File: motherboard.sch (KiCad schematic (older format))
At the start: 90 parts, among them P1 CONN_02X08, U1 STM32F411-LQFP64, U10 74LS125, U11 74LS125, U12 74LS125, U13 74LS125, U14 PCA9517A, U15 PCA9517A, U16 74LS125, U17 74LS125, U2 STM32F411-LQFP64, U3 AP7313, U4 74LS00, U5 74LS125, U6 FM25V20A-G, U7 FM25V20A-G, U8 FM25V20A-G, U9 FM25V20A-G, Y1 32k, Y2 8M(16pF), Y3 32k, Y4 8M(16pF)

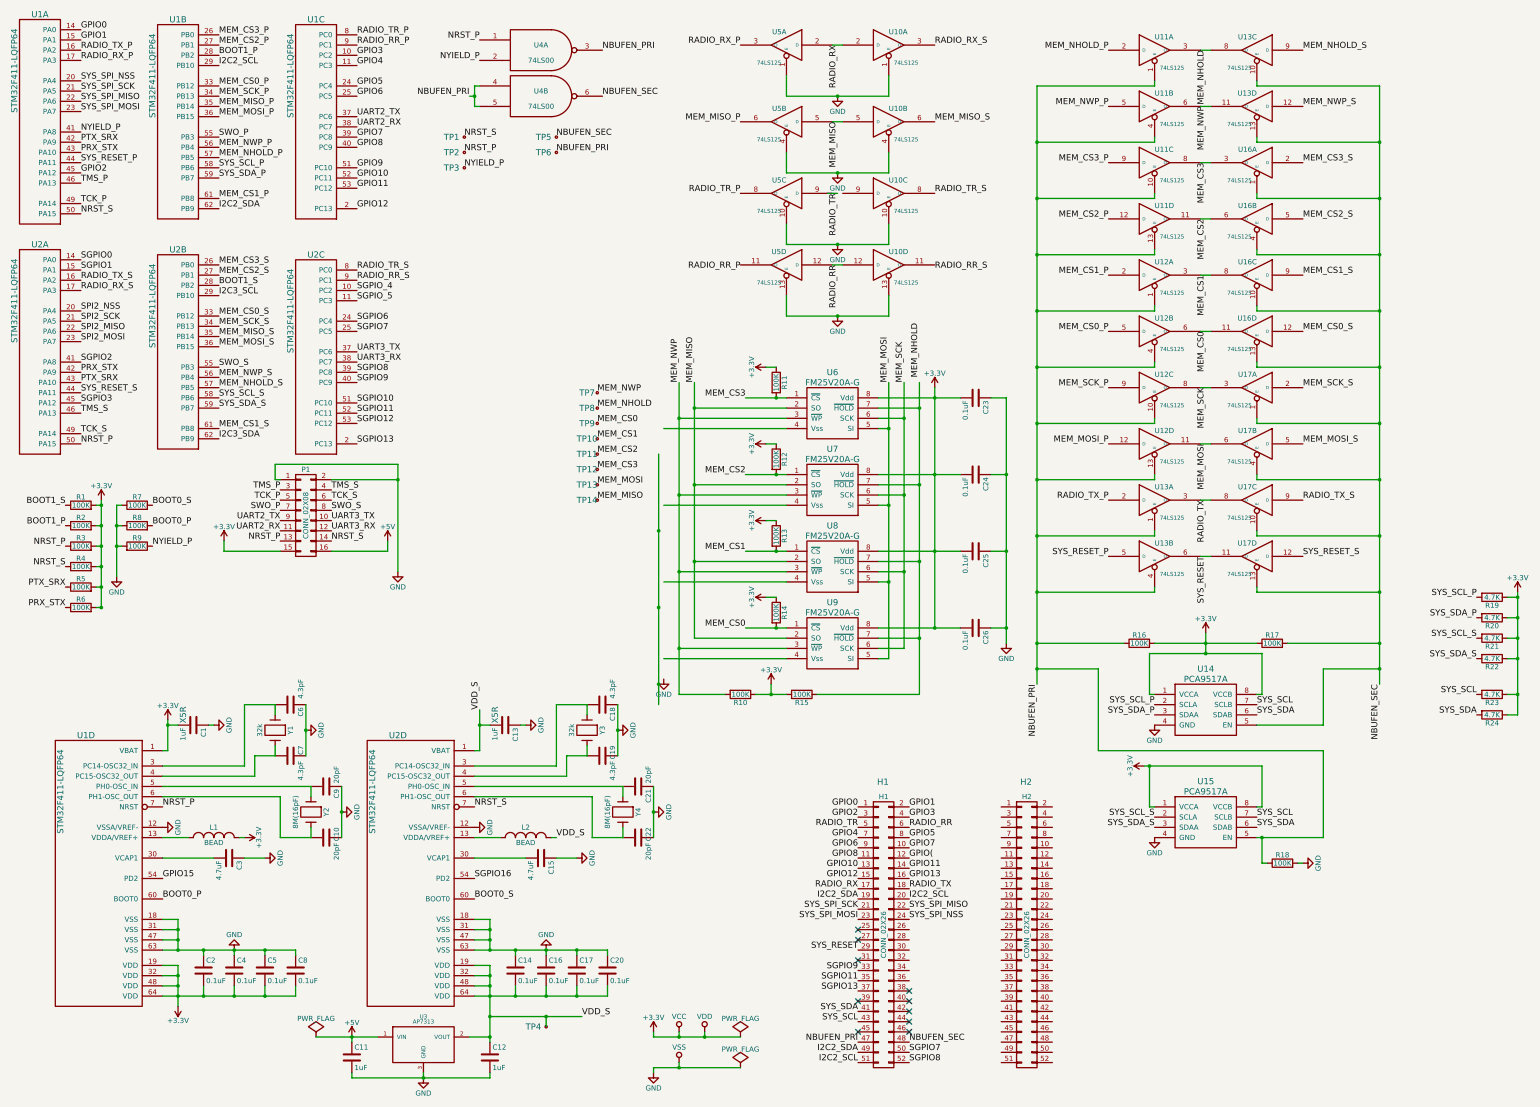
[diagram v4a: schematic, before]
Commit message: Schematic passes DRC
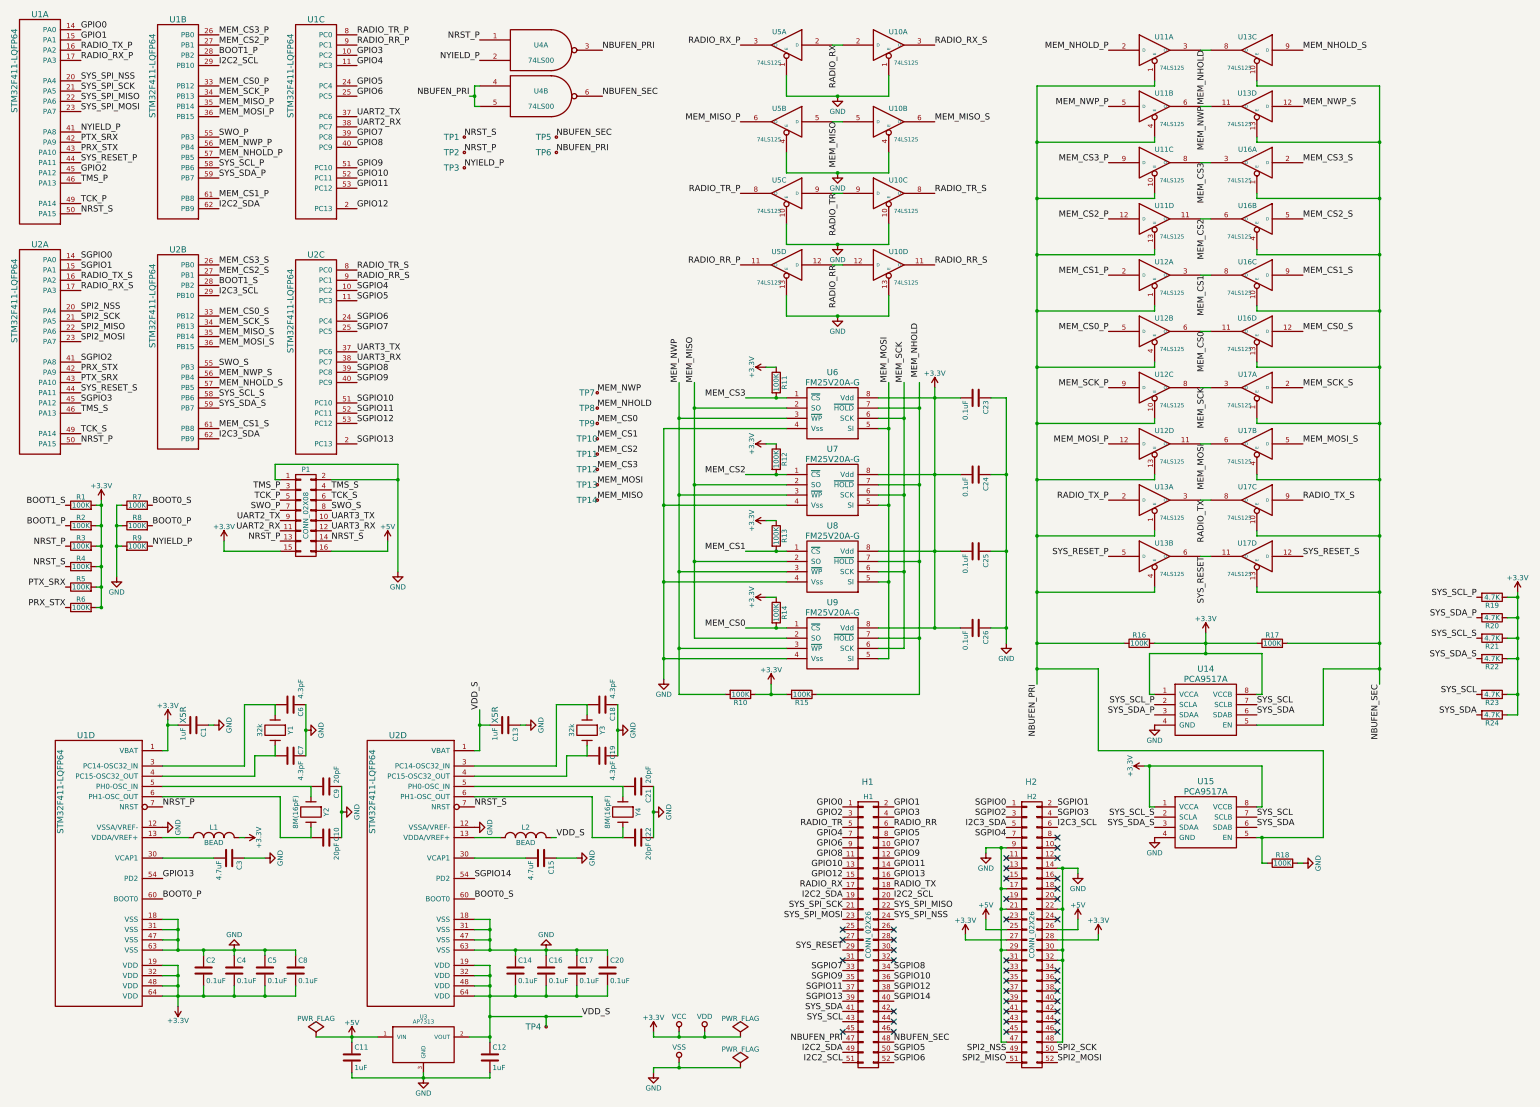
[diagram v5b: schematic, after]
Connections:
- net GPIO( is gone; now on net GPIO9: H1.12 (P12)
- net GPIO15 is gone; now on net GPIO13: U1.54 (PD2)
- net SGPIO16 is gone; now on net SGPIO14: U2.54 (PD2)
- net SGPIO_4 is gone; now on net SGPIO4: U2.10 (PC2)
- net +3V3: now also H2.27 (P27), H2.28 (P28)
- net +5V: now also H2.25 (P25), H2.26 (P26)
- net GND: now also H2.14 (P14), H2.17 (P17), H2.21 (P21), H2.22 (P22), H2.29 (P29), H2.30 (P30), H2.32 (P32), H2.47 (P47), H2.48 (P48), H2.9 (P9), U6.4 (Vss), U7.4 (Vss), U8.4 (Vss), U9.4 (Vss)
- net I2C3_SCL: now also H2.6 (P6)
- net I2C3_SDA: now also H2.5 (P5)
- net RADIO_RR_P: now also U5.11 (O)
- net RADIO_RR_S: now also U10.11 (O)
- net RADIO_TR: now also U10.9 (D), U5.9 (D)
- net SGPIO0: now also H2.1 (P1)
- net SGPIO1: now also H2.2 (P2)
- net SGPIO10: now also H1.36 (P36)
- net SGPIO11: now also H1.37 (P37); no longer H1.35 (P35)
- net SGPIO12: now also H1.38 (P38)
- net SGPIO13: now also H1.39 (P39); no longer H1.37 (P37)
- net SGPIO2: now also H2.3 (P3)
- net SGPIO3: now also H2.4 (P4)
- net SGPIO6: now also H1.52 (P52)
- net SGPIO7: now also H1.33 (P33); no longer H1.50 (P50)
- net SGPIO8: now also H1.34 (P34); no longer H1.52 (P52)
- net SGPIO9: now also H1.35 (P35); no longer H1.33 (P33)
- net SPI2_MISO: now also H2.51 (P51)
- net SPI2_MOSI: now also H2.52 (P52)
- net SPI2_NSS: now also H2.49 (P49)
- net SPI2_SCK: now also H2.50 (P50)
- net SGPIO14: now reaches H1.40 (P40)
- net SGPIO4: now reaches H2.7 (P7)
- net SGPIO_5 renamed SGPIO5
- net SGPIO5: now also H1.50 (P50)
- no-connect marks 10 -> 38
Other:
- moved on the sheet: H1, H2

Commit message: Progress in laying out components
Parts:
- renumbered U17 to U10, U5 to U11, U12 to U11, U13 to U11, U10 to U12, U17 to U12, U11 to U13, U11 to U17, U12 to U17, U13 to U5
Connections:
- net GND: now also U10.10 (E), U10.4 (E), U11.1 (E), U12.1 (E), U5.10 (E), U5.4 (E); no longer U10.10 (E), U10.13 (E), U11.4 (E), U12.4 (E), U5.10 (E), U5.13 (E)
- net MEM_CS0: now also U17.11 (O); no longer U17.6 (O)
- net MEM_CS0_P: now also U17.12 (D); no longer U17.5 (D)
- net MEM_CS1: now also U17.8 (O); no longer U17.3 (O)
- net MEM_CS1_P: now also U17.9 (D); no longer U17.2 (D)
- net MEM_CS2: now also U17.6 (O); no longer U17.11 (O)
- net MEM_CS2_P: now also U17.5 (D); no longer U17.12 (D)
- net MEM_CS3: now also U17.3 (O); no longer U17.8 (O)
- net MEM_CS3_P: now also U17.2 (D); no longer U17.9 (D)
- net MEM_MISO: now also U11.2 (D), U12.2 (D); no longer U11.5 (D), U12.5 (D)
- net MEM_MISO_P: now also U11.3 (O); no longer U11.6 (O)
- net MEM_MISO_S: now also U12.3 (O); no longer U12.6 (O)
- net MEM_MOSI: now also U11.8 (O), U12.8 (O); no longer U11.11 (O), U12.6 (O)
- net MEM_MOSI_P: now also U11.9 (D); no longer U11.12 (D)
- net MEM_MOSI_S: now also U12.9 (D); no longer U12.5 (D)
- net MEM_SCK: now also U11.6 (O), U12.6 (O); no longer U11.8 (O), U12.3 (O)
- net MEM_SCK_P: now also U11.5 (D); no longer U11.9 (D)
- net MEM_SCK_S: now also U12.5 (D); no longer U12.2 (D)
- net NBUFEN_PRI: now also U11.10 (E), U11.13 (E), U11.4 (E), U17.1 (E), U17.10 (E), U17.13 (E), U17.4 (E), U5.13 (E); no longer U11.10 (E), U11.13 (E), U11.4 (E), U17.1 (E), U17.10 (E), U17.13 (E), U17.4 (E), U5.1 (E)
- net NBUFEN_SEC: now also U10.13 (E), U12.10 (E), U12.4 (E); no longer U10.10 (E), U12.1 (E), U12.4 (E)
- net RADIO_RR: now also U10.9 (D), U5.9 (D); no longer U10.12 (D), U5.12 (D)
- net RADIO_RR_P: now also U5.8 (O); no longer U5.11 (O)
- net RADIO_RR_S: now also U10.8 (O); no longer U10.11 (O)
- net RADIO_TR: now also U10.5 (D), U5.5 (D); no longer U10.9 (D), U5.9 (D)
- net RADIO_TR_P: now also U5.6 (O); no longer U5.8 (O)
- net RADIO_TR_S: now also U10.6 (O); no longer U10.8 (O)
- net RADIO_TX: now also U10.11 (O), U5.11 (O); no longer U10.8 (O), U5.3 (O)
- net RADIO_TX_P: now also U5.12 (D); no longer U5.2 (D)
- net RADIO_TX_S: now also U10.12 (D); no longer U10.9 (D)
- net SYS_RESET: now also U11.11 (O); no longer U11.6 (O)
- net SYS_RESET_P: now also U11.12 (D); no longer U11.5 (D)
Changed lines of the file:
@@
 $EndComp
 $Comp
-L 74LS125 U5
-U 2 1 56F0C25F
+L 74LS125 U11
+U 1 1 56F0C25F
 P 8350 1650
-F 0 "U5" H 8350 1750 50  0000 L BNN
+F 0 "U11" H 8350 1750 50  0000 L BNN
 F 1 "74LS125" H 8400 1500 40  0000 L TNN
 F 2 "Housings_SOIC:SOIC-14_3.9x8.7mm_Pitch1.27mm" H 8350 1650 60  0001 C CNN
 F 3 "" H 8350 1650 60  0000 C CNN
-	2    8350 1650
-	-1   0    0    -1
-$EndComp
-$Comp
-L 74LS125 U10
-U 2 1 56F0C346
+	1    8350 1650
+	-1   0    0    -1
+$EndComp
+$Comp
+L 74LS125 U12
+U 1 1 56F0C346
 P 9350 1650
-F 0 "U10" H 9350 1750 50  0000 L BNN
+F 0 "U12" H 9350 1750 50  0000 L BNN
 F 1 "74LS125" H 9400 1500 40  0000 L TNN
 F 2 "Housings_SOIC:SOIC-14_3.9x8.7mm_Pitch1.27mm" H 9350 1650 60  0001 C CNN
 F 3 "" H 9350 1650 60  0000 C CNN
-	2    9350 1650
+	1    9350 1650
 	1    0    0    -1
 $EndComp
@@
 $EndComp
 $Comp
-L 74LS125 U11
+L 74LS125 U13
 U 1 1 56F0DD9C
 P 11950 950
-F 0 "U11" H 11950 1050 50  0000 L BNN
+F 0 "U13" H 11950 1050 50  0000 L BNN
 F 1 "74LS125" H 12000 800 40  0000 L TNN
 F 2 "Housings_SOIC:SOIC-14_3.9x8.7mm_Pitch1.27mm" H 11950 950 60  0001 C CNN
@@
 NYIELD_P
 $Comp
-L 74LS125 U11
+L 74LS125 U13
 U 2 1 56F1CCF5
 P 11950 1500
-F 0 "U11" H 11950 1600 50  0000 L BNN
+F 0 "U13" H 11950 1600 50  0000 L BNN
 F 1 "74LS125" H 12000 1350 40  0000 L TNN
 F 2 "Housings_SOIC:SOIC-14_3.9x8.7mm_Pitch1.27mm" H 11950 1500 60  0001 C CNN
@@
 $EndComp
 $Comp
-L 74LS125 U11
-U 3 1 56F1CE46
+L 74LS125 U17
+U 1 1 56F1CE46
 P 11950 2050
-F 0 "U11" H 11950 2150 50  0000 L BNN
+F 0 "U17" H 11950 2150 50  0000 L BNN
 F 1 "74LS125" H 12000 1900 40  0000 L TNN
 F 2 "Housings_SOIC:SOIC-14_3.9x8.7mm_Pitch1.27mm" H 11950 2050 60  0001 C CNN
 F 3 "" H 11950 2050 60  0000 C CNN
-	3    11950 2050
-	1    0    0    -1
-$EndComp
-$Comp
-L 74LS125 U11
-U 4 1 56F1D346
+	1    11950 2050
+	1    0    0    -1
+$EndComp
+$Comp
+L 74LS125 U17
+U 2 1 56F1D346
 P 11950 2600
-F 0 "U11" H 11950 2700 50  0000 L BNN
+F 0 "U17" H 11950 2700 50  0000 L BNN
 F 1 "74LS125" H 12000 2450 40  0000 L TNN
 F 2 "Housings_SOIC:SOIC-14_3.9x8.7mm_Pitch1.27mm" H 11950 2600 60  0001 C CNN
 F 3 "" H 11950 2600 60  0000 C CNN
-	4    11950 2600
-	1    0    0    -1
-$EndComp
-$Comp
-L 74LS125 U12
-U 1 1 56F1D481
+	2    11950 2600
+	1    0    0    -1
+$EndComp
+$Comp
+L 74LS125 U17
+U 3 1 56F1D481
 P 11950 3150
-F 0 "U12" H 11950 3250 50  0000 L BNN
+F 0 "U17" H 11950 3250 50  0000 L BNN
 F 1 "74LS125" H 12000 3000 40  0000 L TNN
 F 2 "Housings_SOIC:SOIC-14_3.9x8.7mm_Pitch1.27mm" H 11950 3150 60  0001 C CNN
 F 3 "" H 11950 3150 60  0000 C CNN
-	1    11950 3150
-	1    0    0    -1
-$EndComp
-$Comp
-L 74LS125 U12
-U 2 1 56F1D5C5
+	3    11950 3150
+	1    0    0    -1
+$EndComp
+$Comp
+L 74LS125 U17
+U 4 1 56F1D5C5
 P 11950 3700
-F 0 "U12" H 11950 3800 50  0000 L BNN
+F 0 "U17" H 11950 3800 50  0000 L BNN
 F 1 "74LS125" H 12000 3550 40  0000 L TNN
 F 2 "Housings_SOIC:SOIC-14_3.9x8.7mm_Pitch1.27mm" H 11950 3700 60  0001 C CNN
 F 3 "" H 11950 3700 60  0000 C CNN
-	2    11950 3700
-	1    0    0    -1
-$EndComp
-$Comp
-L 74LS125 U12
-U 3 1 56F1DA36
+	4    11950 3700
+	1    0    0    -1
+$EndComp
+$Comp
+L 74LS125 U11
+U 2 1 56F1DA36
 P 11950 4250
-F 0 "U12" H 11950 4350 50  0000 L BNN
+F 0 "U11" H 11950 4350 50  0000 L BNN
 F 1 "74LS125" H 12000 4100 40  0000 L TNN
 F 2 "Housings_SOIC:SOIC-14_3.9x8.7mm_Pitch1.27mm" H 11950 4250 60  0001 C CNN
 F 3 "" H 11950 4250 60  0000 C CNN
-	3    11950 4250
-	1    0    0    -1
-$EndComp
-$Comp
-L 74LS125 U12
-U 4 1 56F1DB80
+	2    11950 4250
+	1    0    0    -1
+$EndComp
+$Comp
+L 74LS125 U11
+U 3 1 56F1DB80
 P 11950 4800
-F 0 "U12" H 11950 4900 50  0000 L BNN
+F 0 "U11" H 11950 4900 50  0000 L BNN
 F 1 "74LS125" H 12000 4650 40  0000 L TNN
 F 2 "Housings_SOIC:SOIC-14_3.9x8.7mm_Pitch1.27mm" H 11950 4800 60  0001 C CNN
 F 3 "" H 11950 4800 60  0000 C CNN
-	4    11950 4800
-	1    0    0    -1
-$EndComp
-$Comp
-L 74LS125 U13
-U 1 1 56F1E3BD
+	3    11950 4800
+	1    0    0    -1
+$EndComp
+$Comp
+L 74LS125 U5
+U 4 1 56F1E3BD
 P 11950 5350
-F 0 "U13" H 11950 5450 50  0000 L BNN
+F 0 "U5" H 11950 5450 50  0000 L BNN
 F 1 "74LS125" H 12000 5200 40  0000 L TNN
 F 2 "Housings_SOIC:SOIC-14_3.9x8.7mm_Pitch1.27mm" H 11950 5350 60  0001 C CNN
 F 3 "" H 11950 5350 60  0000 C CNN
-	1    11950 5350
+	4    11950 5350
 	1    0    0    -1
 $EndComp
@@
 $EndComp
 $Comp
-L 74LS125 U17
-U 1 1 56F39A21
+L 74LS125 U12
+U 2 1 56F39A21
 P 12950 4250
-F 0 "U17" H 12950 4350 50  0000 L BNN
+F 0 "U12" H 12950 4350 50  0000 L BNN
 F 1 "74LS125" H 13000 4100 40  0000 L TNN
 F 2 "Housings_SOIC:SOIC-14_3.9x8.7mm_Pitch1.27mm" H 12950 4250 60  0001 C CNN
 F 3 "" H 12950 4250 60  0000 C CNN
-	1    12950 4250
-	-1   0    0    -1
-$EndComp
-$Comp
-L 74LS125 U17
-U 2 1 56F39B79
+	2    12950 4250
+	-1   0    0    -1
+$EndComp
+$Comp
+L 74LS125 U12
+U 3 1 56F39B79
 P 12950 4800
-F 0 "U17" H 12950 4900 50  0000 L BNN
+F 0 "U12" H 12950 4900 50  0000 L BNN
 F 1 "74LS125" H 13000 4650 40  0000 L TNN
 F 2 "Housings_SOIC:SOIC-14_3.9x8.7mm_Pitch1.27mm" H 12950 4800 60  0001 C CNN
 F 3 "" H 12950 4800 60  0000 C CNN
-	2    12950 4800
-	-1   0    0    -1
-$EndComp
-$Comp
-L 74LS125 U17
-U 3 1 56F3A095
+	3    12950 4800
+	-1   0    0    -1
+$EndComp
+$Comp
+L 74LS125 U10
+U 4 1 56F3A095
 P 12950 5350
-F 0 "U17" H 12950 5450 50  0000 L BNN
+F 0 "U10" H 12950 5450 50  0000 L BNN
 F 1 "74LS125" H 13000 5200 40  0000 L TNN
 F 2 "Housings_SOIC:SOIC-14_3.9x8.7mm_Pitch1.27mm" H 12950 5350 60  0001 C CNN
 F 3 "" H 12950 5350 60  0000 C CNN
-	3    12950 5350
-	-1   0    0    -1
-$EndComp
-$Comp
-L 74LS125 U13
-U 2 1 56F44FCB
+	4    12950 5350
+	-1   0    0    -1
+$EndComp
+$Comp
+L 74LS125 U11
+U 4 1 56F44FCB
 P 11950 5900
-F 0 "U13" H 11950 6000 50  0000 L BNN
+F 0 "U11" H 11950 6000 50  0000 L BNN
 F 1 "74LS125" H 12000 5750 40  0000 L TNN
 F 2 "Housings_SOIC:SOIC-14_3.9x8.7mm_Pitch1.27mm" H 11950 5900 60  0001 C CNN
 F 3 "" H 11950 5900 60  0000 C CNN
-	2    11950 5900
-	1    0    0    -1
-$EndComp
-$Comp
-L 74LS125 U17
+	4    11950 5900
+	1    0    0    -1
+$EndComp
+$Comp
+L 74LS125 U12
 U 4 1 56F45134
 P 12950 5900
-F 0 "U17" H 12950 6000 50  0000 L BNN
+F 0 "U12" H 12950 6000 50  0000 L BNN
 F 1 "74LS125" H 13000 5750 40  0000 L TNN
 F 2 "Housings_SOIC:SOIC-14_3.9x8.7mm_Pitch1.27mm" H 12950 5900 60  0001 C CNN
@@
 $Comp
 L 74LS125 U5
-U 4 1 583EB409
+U 3 1 583EB409
 P 8350 3050
 F 0 "U5" H 8350 3150 50  0000 L BNN
@@
 F 2 "Housings_SOIC:SOIC-14_3.9x8.7mm_Pitch1.27mm" H 8350 3050 60  0001 C CNN
 F 3 "" H 8350 3050 60  0000 C CNN
-	4    8350 3050
+	3    8350 3050
 	-1   0    0    -1
 $EndComp
 $Comp
 L 74LS125 U5
-U 3 1 583EB40F
+U 2 1 583EB40F
 P 8350 2350
 F 0 "U5" H 8350 2450 50  0000 L BNN
@@
 F 2 "Housings_SOIC:SOIC-14_3.9x8.7mm_Pitch1.27mm" H 8350 2350 60  0001 C CNN
 F 3 "" H 8350 2350 60  0000 C CNN
-	3    8350 2350
+	2    8350 2350
 	-1   0    0    -1
 $EndComp
 $Comp
 L 74LS125 U10
-U 3 1 583EB415
+U 2 1 583EB415
 P 9350 2350
 F 0 "U10" H 9350 2450 50  0000 L BNN
@@
 F 2 "Housings_SOIC:SOIC-14_3.9x8.7mm_Pitch1.27mm" H 9350 2350 60  0001 C CNN
 F 3 "" H 9350 2350 60  0000 C CNN
-	3    9350 2350
+	2    9350 2350
 	1    0    0    -1
 $EndComp
 $Comp
 L 74LS125 U10
-U 4 1 583EB41B
+U 3 1 583EB41B
 P 9350 3050
 F 0 "U10" H 9350 3150 50  0000 L BNN
@@
 F 2 "Housings_SOIC:SOIC-14_3.9x8.7mm_Pitch1.27mm" H 9350 3050 60  0001 C CNN
 F 3 "" H 9350 3050 60  0000 C CNN
-	4    9350 3050
-	1    0    0    -1
-$EndComp
+	3    9350 3050
+	1    0    0    -1
+$EndComp
